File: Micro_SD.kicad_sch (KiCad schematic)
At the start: 3 parts, among them J2 DM3BT-DSF-PEJS

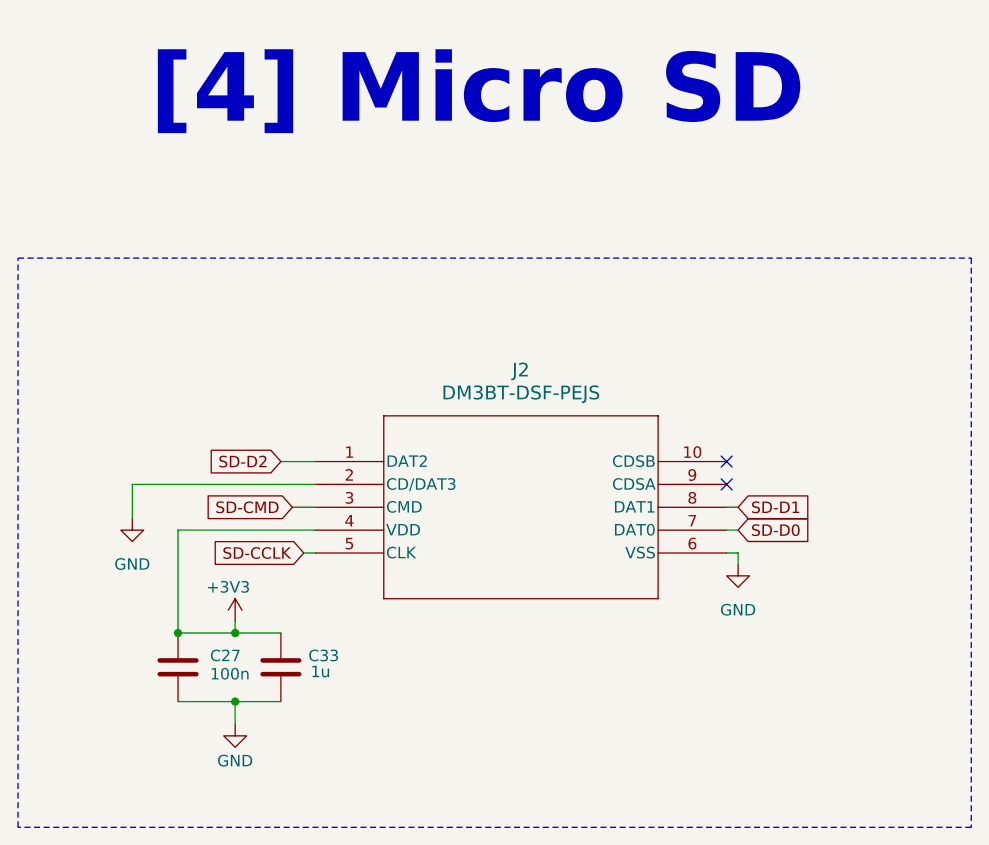
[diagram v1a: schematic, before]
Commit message: Added Level Shifter for SD card
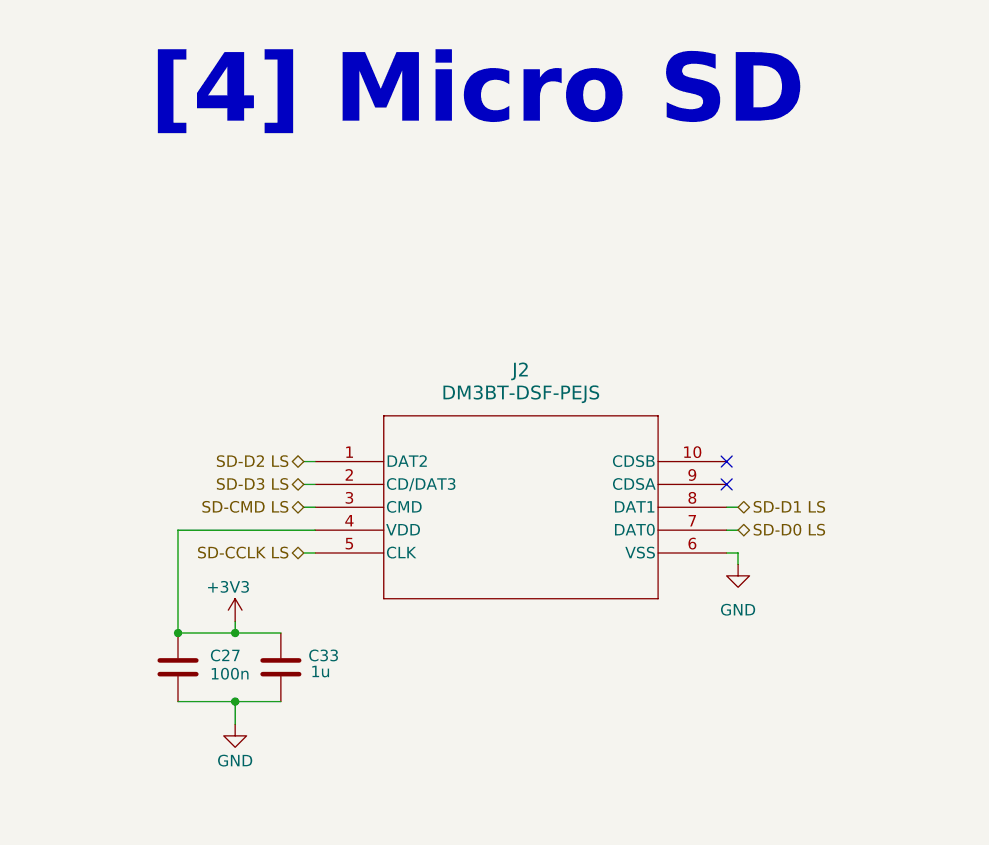
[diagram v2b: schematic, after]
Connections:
- net GND: no longer J2.2 (CD/DAT3)
- net SD-CCLK renamed SD-CCLK LS
- net SD-CMD renamed SD-CMD LS
- net SD-D0 renamed SD-D0 LS
- net SD-D1 renamed SD-D1 LS
- net SD-D2 renamed SD-D2 LS
- new net SD-D3 LS: J2.2 (CD/DAT3)
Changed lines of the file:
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@@
 	(generator_version "10.0")
 	(paper "A4")
-	(rectangle
-		(start 95.25 47.244)
-		(end 201.168 110.49)
-		(stroke
-			(width 0)
-			(type dash)
-		)
-		(fill
-			(type none)
-		)
-	)
 	(text "[4] Micro SD"
 		(exclude_from_sim no)
@@
 	(wire
 		(pts
-			(xy 125.73 74.93) (xy 128.27 74.93)
+			(xy 127 74.93) (xy 128.27 74.93)
 		)
 		(stroke
@@
 	(wire
 		(pts
-			(xy 128.27 72.39) (xy 107.95 72.39)
-		)
-		(stroke
-			(width 0)
-			(type default)
-		)
-	)
-	(wire
-		(pts
 			(xy 127 80.01) (xy 128.27 80.01)
 		)
@@
 	(wire
 		(pts
+			(xy 127 72.39) (xy 128.27 72.39)
+		)
+		(stroke
+			(width 0)
+			(type default)
+		)
+	)
+	(wire
+		(pts
 			(xy 113.03 77.47) (xy 113.03 88.9)
 		)
@@
 	(wire
 		(pts
-			(xy 124.46 69.85) (xy 128.27 69.85)
+			(xy 127 69.85) (xy 128.27 69.85)
 		)
 		(stroke
@@
 	(wire
 		(pts
-			(xy 107.95 72.39) (xy 107.95 76.2)
-		)
-		(stroke
-			(width 0)
-			(type default)
-		)
-	)
-	(wire
-		(pts
 			(xy 173.99 74.93) (xy 175.26 74.93)
 		)
@@
 		)
 	)
-	(global_label "SD-CMD"
-		(shape input)
-		(at 125.73 74.93 180)
-		(fields_autoplaced yes)
-		(effects
-			(font
-				(size 1.27 1.27)
-			)
-			(justify right)
-		)
-		(property "Intersheetrefs" "${INTERSHEET_REFS}"
-			(at 114.7015 74.93 0)
-			(hide yes)
-			(show_name no)
-			(do_not_autoplace no)
-			(effects
-				(font
-					(size 1.27 1.27)
-				)
-				(justify right)
-			)
-		)
-	)
-	(global_label "SD-D0"
-		(shape input)
+	(hierarchical_label "SD-D0 LS"
+		(shape bidirectional)
 		(at 175.26 77.47 0)
-		(fields_autoplaced yes)
 		(effects
 			(font
@@
 			(justify left)
 		)
-		(property "Intersheetrefs" "${INTERSHEET_REFS}"
-			(at 184.7766 77.47 0)
-			(hide yes)
-			(show_name no)
-			(do_not_autoplace no)
-			(effects
-				(font
-					(size 1.27 1.27)
-				)
-				(justify left)
-			)
-		)
-	)
-	(global_label "SD-CCLK"
-		(shape input)
+	)
+	(hierarchical_label "SD-D2 LS"
+		(shape bidirectional)
+		(at 127 69.85 180)
+		(effects
+			(font
+				(size 1.27 1.27)
+			)
+			(justify right)
+		)
+	)
+	(hierarchical_label "SD-CMD LS"
+		(shape bidirectional)
+		(at 127 74.93 180)
+		(effects
+			(font
+				(size 1.27 1.27)
+			)
+			(justify right)
+		)
+	)
+	(hierarchical_label "SD-D3 LS"
+		(shape bidirectional)
+		(at 127 72.39 180)
+		(effects
+			(font
+				(size 1.27 1.27)
+			)
+			(justify right)
+		)
+	)
+	(hierarchical_label "SD-D1 LS"
+		(shape bidirectional)
+		(at 175.26 74.93 0)
+		(effects
+			(font
+				(size 1.27 1.27)
+			)
+			(justify left)
+		)
+	)
+	(hierarchical_label "SD-CCLK LS"
+		(shape bidirectional)
 		(at 127 80.01 180)
-		(fields_autoplaced yes)
-		(effects
-			(font
-				(size 1.27 1.27)
-			)
-			(justify right)
-		)
-		(property "Intersheetrefs" "${INTERSHEET_REFS}"
-			(at 115.1248 80.01 0)
-			(hide yes)
-			(show_name no)
-			(do_not_autoplace no)
-			(effects
-				(font
-					(size 1.27 1.27)
-				)
-				(justify right)
-			)
-		)
-	)
-	(global_label "SD-D1"
-		(shape input)
-		(at 175.26 74.93 0)
-		(fields_autoplaced yes)
-		(effects
-			(font
-				(size 1.27 1.27)
-			)
-			(justify left)
-		)
-		(property "Intersheetrefs" "${INTERSHEET_REFS}"
-			(at 184.7766 74.93 0)
-			(hide yes)
-			(show_name no)
-			(do_not_autoplace no)
-			(effects
-				(font
-					(size 1.27 1.27)
-				)
-				(justify left)
-			)
-		)
-	)
-	(global_label "SD-D2"
-		(shape input)
-		(at 124.46 69.85 180)
-		(fields_autoplaced yes)
-		(effects
-			(font
-				(size 1.27 1.27)
-			)
-			(justify right)
-		)
-		(property "Intersheetrefs" "${INTERSHEET_REFS}"
-			(at 114.9434 69.85 0)
-			(hide yes)
-			(show_name no)
-			(do_not_autoplace no)
-			(effects
-				(font
-					(size 1.27 1.27)
-				)
-				(justify right)
-			)
-		)
-	)
-	(symbol
-		(lib_id "power:GND")
-		(at 107.95 76.2 0)
-		(unit 1)
-		(body_style 1)
-		(exclude_from_sim no)
-		(in_bom yes)
-		(on_board yes)
-		(in_pos_files yes)
-		(dnp no)
-		(fields_autoplaced yes)
-		(property "Reference" "#PWR025"
-			(at 107.95 82.55 0)
-			(hide yes)
-			(show_name no)
-			(do_not_autoplace no)
-			(effects
-				(font
-					(size 1.27 1.27)
-				)
-			)
-		)
-		(property "Value" "GND"
-			(at 107.95 81.28 0)
-			(show_name no)
-			(do_not_autoplace no)
-			(effects
-				(font
-					(size 1.27 1.27)
-				)
-			)
-		)
-		(property "Footprint" ""
-			(at 107.95 76.2 0)
-			(hide yes)
-			(show_name no)
-			(do_not_autoplace no)
-			(effects
-				(font
-					(size 1.27 1.27)
-				)
-			)
-		)
-		(property "Datasheet" ""
-			(at 107.95 76.2 0)
-			(hide yes)
-			(show_name no)
-			(do_not_autoplace no)
-			(effects
-				(font
-					(size 1.27 1.27)
-				)
-			)
-		)
-		(property "Description" "Power symbol creates a global label with name \"GND\" , ground"
-			(at 107.95 76.2 0)
-			(hide yes)
-			(show_name no)
-			(do_not_autoplace no)
-			(effects
-				(font
-					(size 1.27 1.27)
-				)
-			)
-		)
-		(pin "1"
-		)
-		(instances
-			(project "adapter-pcb"
-				(path "/94da9b83-1146-4f01-8e34-8153765b0257/1213a66d-8b93-46c4-b414-9452953a635e"
-					(reference "#PWR025")
-					(unit 1)
-				)
-			)
-		)
-	)
+		(effects
+			(font
+				(size 1.27 1.27)
+			)
+			(justify right)
+		)
+	)

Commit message: Added pcb files for ethernet breakout board
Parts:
- J2: External Part Number (none) -> 798-DM3BT-DSF-PEJS; MPN (none) -> C597972
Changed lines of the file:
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@@
+			)
+		)
+		(property "External Part Number" ""
+			(at 113.03 92.71 0)
+			(hide yes)
+			(show_name no)
+			(do_not_autoplace no)
+			(effects
+				(font
+					(size 1.27 1.27)
+				)
+			)
+		)
+		(property "MPN" ""
+			(at 113.03 92.71 0)
+			(hide yes)
+			(show_name no)
+			(do_not_autoplace no)
+			(effects
+				(font
+					(size 1.27 1.27)
+				)
 			)
 		)
@@
 			)
 		)
-		(property "Datasheet" "DM3BT-DSF-PEJS"
+		(property "Datasheet" "https://www.hirose.com/en/product/document?clcode=CL0609-0029-9-00&productname=DM3BT-DSF-PEJS&series=DM3&documenttype=Catalog&lang=en&documentid=D49662_en"
 			(at 128.27 69.85 0)
 			(hide yes)
@@
 		)
 		(property "MANUFACTURER_PART_NUMBER" "DM3BT-DSF-PEJS"
+			(at 128.27 69.85 0)
+			(hide yes)
+			(show_name no)
+			(do_not_autoplace no)
+			(effects
+				(font
+					(size 1.27 1.27)
+				)
+			)
+		)
+		(property "External Part Number" "798-DM3BT-DSF-PEJS "
+			(at 128.27 69.85 0)
+			(hide yes)
+			(show_name no)
+			(do_not_autoplace no)
+			(effects
+				(font
+					(size 1.27 1.27)
+				)
+			)
+		)
+		(property "MPN" "C597972"
 			(at 128.27 69.85 0)
 			(hide yes)
@@
 			(at 124.46 92.71 0)
 			(hide yes)
+			(show_name no)
+			(do_not_autoplace no)
+			(effects
+				(font
+					(size 1.27 1.27)
+				)
+			)
+		)
+		(property "External Part Number" ""
+			(at 124.46 92.71 0)
+			(hide yes)
+			(show_name no)
+			(do_not_autoplace no)
+			(effects
+				(font
+					(size 1.27 1.27)
+				)
+			)
+		)
+		(property "MPN" ""
+			(at 124.46 92.71 0)
+			(hide yes)

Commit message: Updated BOM and added fiducials
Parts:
- C27: External Part Number (none) -> GCM188R71H104KA57J; MANUFACTURER_PART_NUMBER GCM155R71H104KE02D -> (none); MPN (none) -> C3011652
- C33: External Part Number (none) -> GCM21BR71H105KA03L; MANUFACTURER_PART_NUMBER GRT155R61A105KE01D -> (none); MPN (none) -> C126592
- J2: External Part Number 798-DM3BT-DSF-PEJS -> DM3BT-DSF-PEJS; MANUFACTURER_PART_NUMBER DM3BT-DSF-PEJS -> (none)
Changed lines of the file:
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@@
 			)
 		)
-		(property "MANUFACTURER_PART_NUMBER" "GCM155R71H104KE02D"
+		(property "External Part Number" "GCM188R71H104KA57J"
 			(at 113.03 92.71 0)
 			(hide yes)
@@
 			)
 		)
-		(property "External Part Number" ""
-			(at 113.03 92.71 0)
-			(hide yes)
-			(show_name no)
-			(do_not_autoplace no)
-			(effects
-				(font
-					(size 1.27 1.27)
-				)
-			)
-		)
-		(property "MPN" ""
+		(property "MPN" "C3011652"
 			(at 113.03 92.71 0)
 			(hide yes)
@@
 			)
 		)
-		(property "MANUFACTURER_PART_NUMBER" "DM3BT-DSF-PEJS"
-			(at 128.27 69.85 0)
-			(hide yes)
-			(show_name no)
-			(do_not_autoplace no)
-			(effects
-				(font
-					(size 1.27 1.27)
-				)
-			)
-		)
-		(property "External Part Number" "798-DM3BT-DSF-PEJS "
+		(property "External Part Number" "DM3BT-DSF-PEJS"
 			(at 128.27 69.85 0)
 			(hide yes)
@@
 			)
 		)
-		(property "MANUFACTURER_PART_NUMBER" "GRT155R61A105KE01D"
-			(at 124.46 92.71 0)
-			(hide yes)
-			(show_name no)
-			(do_not_autoplace no)
-			(effects
-				(font
-					(size 1.27 1.27)
-				)
-			)
-		)
-		(property "External Part Number" ""
-			(at 124.46 92.71 0)
-			(hide yes)
-			(show_name no)
-			(do_not_autoplace no)
-			(effects
-				(font
-					(size 1.27 1.27)
-				)
-			)
-		)
-		(property "MPN" ""
-			(at 124.46 92.71 0)
-			(hide yes)
+		(property "External Part Number" "GCM21BR71H105KA03L"
+			(at 124.46 92.71 0)
+			(hide yes)
+			(show_name no)
+			(do_not_autoplace no)
+			(effects
+				(font
+					(size 1.27 1.27)
+				)
+			)
+		)
+		(property "MPN" "C126592"
+			(at 124.46 92.71 0)
+			(hide yes)

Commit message: added solder bridges and updated BOM
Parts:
- C27: External Part Num (none) -> C3011652; External Part Number GCM188R71H104KA57J -> (none); MPN C3011652 -> GCM188R71H104KA57J
- C33: External Part Num (none) -> C126592; External Part Number GCM21BR71H105KA03L -> (none); MPN C126592 -> GCM21BR71H105KA03L
- J2: External Part Num (none) -> C597972; External Part Number DM3BT-DSF-PEJS -> (none); MPN C597972 -> DM3BT-DSF-PEJS
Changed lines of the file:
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@@
 			)
 		)
-		(property "External Part Number" "GCM188R71H104KA57J"
+		(property "MPN" "GCM188R71H104KA57J"
 			(at 113.03 92.71 0)
 			(hide yes)
@@
 			)
 		)
-		(property "MPN" "C3011652"
+		(property "External Part Num" "C3011652"
 			(at 113.03 92.71 0)
 			(hide yes)
@@
 			)
 		)
-		(property "External Part Number" "DM3BT-DSF-PEJS"
-			(at 128.27 69.85 0)
-			(hide yes)
-			(show_name no)
-			(do_not_autoplace no)
-			(effects
-				(font
-					(size 1.27 1.27)
-				)
-			)
-		)
-		(property "MPN" "C597972"
+		(property "MPN" "DM3BT-DSF-PEJS"
+			(at 128.27 69.85 0)
+			(hide yes)
+			(show_name no)
+			(do_not_autoplace no)
+			(effects
+				(font
+					(size 1.27 1.27)
+				)
+			)
+		)
+		(property "External Part Num" "C597972"
 			(at 128.27 69.85 0)
 			(hide yes)
@@
 			)
 		)
-		(property "External Part Number" "GCM21BR71H105KA03L"
-			(at 124.46 92.71 0)
-			(hide yes)
-			(show_name no)
-			(do_not_autoplace no)
-			(effects
-				(font
-					(size 1.27 1.27)
-				)
-			)
-		)
-		(property "MPN" "C126592"
-			(at 124.46 92.71 0)
-			(hide yes)
+		(property "MPN" "GCM21BR71H105KA03L"
+			(at 124.46 92.71 0)
+			(hide yes)
+			(show_name no)
+			(do_not_autoplace no)
+			(effects
+				(font
+					(size 1.27 1.27)
+				)
+			)
+		)
+		(property "External Part Num" "C126592"
+			(at 124.46 92.71 0)
+			(hide yes)
